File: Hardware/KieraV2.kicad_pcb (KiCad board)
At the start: 2 copper layers, 111 x 63.2 mm, 110 parts, among them J1 Conn_01x04_Male, J2 Conn_01x06_Male, SW1 SW_Rotary2x4, SW10 SW_Push, SW11 SW_Push, SW2 SW_Rotary2x4, SW3 SW_Push, SW4 SW_Push, SW5 SW_Push, SW6 SW_Push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

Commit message: refilled gnd again
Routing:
- net GND: vias 90 -> 171
- net (no net): vias 0 -> 11
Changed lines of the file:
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@@
     (thickness 1.6)
     (drawings 31)
-    (tracks 767)
+    (tracks 860)
     (zones 0)
     (modules 110)
@@
   (gr_line (start 105.5 89.8) (end 210.5 89.8) (layer Edge.Cuts) (width 0.1))
   (gr_line (start 102.5 92.8) (end 102.5 150) (layer Edge.Cuts) (width 0.1))
+  (via (at 191.99 94.025) (size 0.8) (drill 0.4) (layers F.Cu B.Cu) (net 0))
+  (via (at 195.01 95.565) (size 0.8) (drill 0.4) (layers F.Cu B.Cu) (net 0))
+  (via (at 197 92.575) (size 0.8) (drill 0.4) (layers F.Cu B.Cu) (net 0))
+  (via (at 188.02 92.875) (size 0.8) (drill 0.4) (layers F.Cu B.Cu) (net 0))
+  (via (at 191.11 99.015) (size 0.8) (drill 0.4) (layers F.Cu B.Cu) (net 0))
+  (via (at 186.3 99.505) (size 0.8) (drill 0.4) (layers F.Cu B.Cu) (net 0))
+  (via (at 183.16 99.015) (size 0.8) (drill 0.4) (layers F.Cu B.Cu) (net 0))
+  (via (at 175.51 105.285) (size 0.8) (drill 0.4) (layers F.Cu B.Cu) (net 0))
+  (via (at 180.14 105.205) (size 0.8) (drill 0.4) (layers F.Cu B.Cu) (net 0))
+  (via (at 209.89 92.025) (size 0.8) (drill 0.4) (layers F.Cu B.Cu) (net 0))
+  (via (at 175.59 112.12) (size 0.8) (drill 0.4) (layers F.Cu B.Cu) (net 0))
   (segment (start 154.6 109.840702) (end 154.6 109.8) (width 0.25) (layer F.Cu) (net 1))
   (segment (start 155.884298 111.125) (end 154.6 109.840702) (width 0.25) (layer F.Cu) (net 1))
@@
   (segment (start 151.3 109.8) (end 149.97 109.8) (width 0.25) (layer F.Cu) (net 1))
   (segment (start 149.97 109.8) (end 149.76 110.01) (width 0.25) (layer F.Cu) (net 1))
+  (via (at 149.19 111.42) (size 0.8) (drill 0.4) (layers F.Cu B.Cu) (net 1))
+  (via (at 152.25 112.7) (size 0.8) (drill 0.4) (layers F.Cu B.Cu) (net 1))
+  (via (at 150.04 112.25) (size 0.8) (drill 0.4) (layers F.Cu B.Cu) (net 1))
+  (via (at 146.75 107.96) (size 0.8) (drill 0.4) (layers F.Cu B.Cu) (net 1))
+  (via (at 153.77 107.32) (size 0.8) (drill 0.4) (layers F.Cu B.Cu) (net 1))
+  (via (at 159.25 110.81) (size 0.8) (drill 0.4) (layers F.Cu B.Cu) (net 1))
+  (via (at 161.5 110.93) (size 0.8) (drill 0.4) (layers F.Cu B.Cu) (net 1))
+  (via (at 163.06 108.61) (size 0.8) (drill 0.4) (layers F.Cu B.Cu) (net 1))
+  (via (at 163.36 105.59) (size 0.8) (drill 0.4) (layers F.Cu B.Cu) (net 1))
+  (via (at 166.05 105.71) (size 0.8) (drill 0.4) (layers F.Cu B.Cu) (net 1))
+  (via (at 166.4 109.16) (size 0.8) (drill 0.4) (layers F.Cu B.Cu) (net 1))
+  (via (at 170.35 113.1) (size 0.8) (drill 0.4) (layers F.Cu B.Cu) (net 1))
+  (via (at 173.99 112.24) (size 0.8) (drill 0.4) (layers F.Cu B.Cu) (net 1))
+  (via (at 180.39 114.37) (size 0.8) (drill 0.4) (layers F.Cu B.Cu) (net 1))
+  (via (at 178.5 115.94) (size 0.8) (drill 0.4) (layers F.Cu B.Cu) (net 1))
+  (via (at 180.47 119.08) (size 0.8) (drill 0.4) (layers F.Cu B.Cu) (net 1))
+  (via (at 178.55 121.98) (size 0.8) (drill 0.4) (layers F.Cu B.Cu) (net 1))
+  (via (at 178.28 118.11) (size 0.8) (drill 0.4) (layers F.Cu B.Cu) (net 1))
+  (via (at 181.4 124.85) (size 0.8) (drill 0.4) (layers F.Cu B.Cu) (net 1))
+  (via (at 179.48 128.08) (size 0.8) (drill 0.4) (layers F.Cu B.Cu) (net 1))
+  (via (at 183.48 133.02) (size 0.8) (drill 0.4) (layers F.Cu B.Cu) (net 1))
+  (via (at 182.27 140.23) (size 0.8) (drill 0.4) (layers F.Cu B.Cu) (net 1))
+  (via (at 190.15 135.41) (size 0.8) (drill 0.4) (layers F.Cu B.Cu) (net 1))
+  (via (at 186.54 148.22) (size 0.8) (drill 0.4) (layers F.Cu B.Cu) (net 1))
+  (via (at 175.85 148.11) (size 0.8) (drill 0.4) (layers F.Cu B.Cu) (net 1))
+  (via (at 176.24 142.67) (size 0.8) (drill 0.4) (layers F.Cu B.Cu) (net 1))
+  (via (at 169.76 149.71) (size 0.8) (drill 0.4) (layers F.Cu B.Cu) (net 1))
+  (via (at 155.43 145.36) (size 0.8) (drill 0.4) (layers F.Cu B.Cu) (net 1))
+  (via (at 158.77 139.17) (size 0.8) (drill 0.4) (layers F.Cu B.Cu) (net 1))
+  (via (at 160.73 145.25) (size 0.8) (drill 0.4) (layers F.Cu B.Cu) (net 1))
+  (via (at 132.46 149.4) (size 0.8) (drill 0.4) (layers F.Cu B.Cu) (net 1))
+  (via (at 112.33 141.63) (size 0.8) (drill 0.4) (layers F.Cu B.Cu) (net 1))
+  (via (at 125.62 137.12) (size 0.8) (drill 0.4) (layers F.Cu B.Cu) (net 1))
+  (via (at 126.77 132.24) (size 0.8) (drill 0.4) (layers F.Cu B.Cu) (net 1))
+  (via (at 126.69 128.51) (size 0.8) (drill 0.4) (layers F.Cu B.Cu) (net 1))
+  (via (at 136.73 119) (size 0.8) (drill 0.4) (layers F.Cu B.Cu) (net 1))
+  (via (at 138.86 117.35) (size 0.8) (drill 0.4) (layers F.Cu B.Cu) (net 1))
+  (via (at 133.39 112.55) (size 0.8) (drill 0.4) (layers F.Cu B.Cu) (net 1))
+  (via (at 132.83 108.85) (size 0.8) (drill 0.4) (layers F.Cu B.Cu) (net 1))
+  (via (at 135.32 110.39) (size 0.8) (drill 0.4) (layers F.Cu B.Cu) (net 1))
+  (via (at 139.98 109.63) (size 0.8) (drill 0.4) (layers F.Cu B.Cu) (net 1))
+  (via (at 143.88 108.01) (size 0.8) (drill 0.4) (layers F.Cu B.Cu) (net 1))
+  (via (at 138.91 98.13) (size 0.8) (drill 0.4) (layers F.Cu B.Cu) (net 1))
+  (via (at 144.92 98.19) (size 0.8) (drill 0.4) (layers F.Cu B.Cu) (net 1))
+  (via (at 152.35 91.68) (size 0.8) (drill 0.4) (layers F.Cu B.Cu) (net 1))
+  (via (at 148.73 91.01) (size 0.8) (drill 0.4) (layers F.Cu B.Cu) (net 1))
+  (via (at 173.55 93.2) (size 0.8) (drill 0.4) (layers F.Cu B.Cu) (net 1))
+  (via (at 176.47 99.06) (size 0.8) (drill 0.4) (layers F.Cu B.Cu) (net 1))
+  (via (at 179.58 98.84) (size 0.8) (drill 0.4) (layers F.Cu B.Cu) (net 1))
+  (via (at 183.9 92.67) (size 0.8) (drill 0.4) (layers F.Cu B.Cu) (net 1))
+  (via (at 188.81 106.6) (size 0.8) (drill 0.4) (layers F.Cu B.Cu) (net 1))
+  (via (at 194.53 110.25) (size 0.8) (drill 0.4) (layers F.Cu B.Cu) (net 1))
+  (via (at 196.63 113.08) (size 0.8) (drill 0.4) (layers F.Cu B.Cu) (net 1))
+  (via (at 194.05 114.49) (size 0.8) (drill 0.4) (layers F.Cu B.Cu) (net 1))
+  (via (at 196.6 122.9) (size 0.8) (drill 0.4) (layers F.Cu B.Cu) (net 1))
+  (via (at 199.35 125.25) (size 0.8) (drill 0.4) (layers F.Cu B.Cu) (net 1))
+  (via (at 210.15 126.15) (size 0.8) (drill 0.4) (layers F.Cu B.Cu) (net 1))
+  (via (at 210.46 134.85) (size 0.8) (drill 0.4) (layers F.Cu B.Cu) (net 1))
+  (via (at 203.33 131.85) (size 0.8) (drill 0.4) (layers F.Cu B.Cu) (net 1))
+  (via (at 199.49 141.66) (size 0.8) (drill 0.4) (layers F.Cu B.Cu) (net 1))
+  (via (at 197.11 147.66) (size 0.8) (drill 0.4) (layers F.Cu B.Cu) (net 1))
+  (via (at 191.86 121.55) (size 0.8) (drill 0.4) (layers F.Cu B.Cu) (net 1))
+  (via (at 211.03 105.16) (size 0.8) (drill 0.4) (layers F.Cu B.Cu) (net 1))
+  (via (at 210.39 96.51) (size 0.8) (drill 0.4) (layers F.Cu B.Cu) (net 1))
+  (via (at 188.8 97.29) (size 0.8) (drill 0.4) (layers F.Cu B.Cu) (net 1))
+  (via (at 193.27 95.32) (size 0.8) (drill 0.4) (layers F.Cu B.Cu) (net 1))
+  (via (at 197.42 96.02) (size 0.8) (drill 0.4) (layers F.Cu B.Cu) (net 1))
+  (via (at 186.96 94.39) (size 0.8) (drill 0.4) (layers F.Cu B.Cu) (net 1))
+  (via (at 194.77 102.24) (size 0.8) (drill 0.4) (layers F.Cu B.Cu) (net 1))
+  (via (at 124.21 105.41) (size 0.8) (drill 0.4) (layers F.Cu B.Cu) (net 1))
+  (via (at 125.85 100.57) (size 0.8) (drill 0.4) (layers F.Cu B.Cu) (net 1))
+  (via (at 129.22 101.27) (size 0.8) (drill 0.4) (layers F.Cu B.Cu) (net 1))
+  (via (at 124.07 96.5) (size 0.8) (drill 0.4) (layers F.Cu B.Cu) (net 1))
+  (via (at 121.36 92.48) (size 0.8) (drill 0.4) (layers F.Cu B.Cu) (net 1))
+  (via (at 128.91 92.53) (size 0.8) (drill 0.4) (layers F.Cu B.Cu) (net 1))
+  (via (at 124.67 112.26) (size 0.8) (drill 0.4) (layers F.Cu B.Cu) (net 1))
+  (via (at 119.31 116.74) (size 0.8) (drill 0.4) (layers F.Cu B.Cu) (net 1))
+  (via (at 119.68 124.22) (size 0.8) (drill 0.4) (layers F.Cu B.Cu) (net 1))
+  (via (at 110.38 115.06) (size 0.8) (drill 0.4) (layers F.Cu B.Cu) (net 1))
+  (via (at 113.51 127.66) (size 0.8) (drill 0.4) (layers F.Cu B.Cu) (net 1))
+  (via (at 115.12 124.5) (size 0.8) (drill 0.4) (layers F.Cu B.Cu) (net 1))
   (segment (start 152.525 104.775) (end 152.85 105.1) (width 0.25) (layer F.Cu) (net 2))
   (segment (start 151.05 104.775) (end 152.525 104.775) (width 0.25) (layer F.Cu) (net 2))
@@
   (segment (start 183.39 100.835) (end 191.725 92.5) (width 0.25) (layer F.Cu) (net 83))
   (segment (start 183.39 103.09) (end 183.39 100.835) (width 0.25) (layer F.Cu) (net 83))
-  (segment (start 193.55 95.875) (end 195.075 97.4) (width 0.25) (layer F.Cu) (net 84))
-  (segment (start 191.75 95.875) (end 193.55 95.875) (width 0.25) (layer F.Cu) (net 84))
   (segment (start 195.075 97.4) (end 196.75 97.4) (width 0.25) (layer F.Cu) (net 84))
   (via (at 172.25 110.191646) (size 0.8) (drill 0.4) (layers F.Cu B.Cu) (net 84))
@@
   (segment (start 171.7899 110.191646) (end 171.698263 110.100009) (width 0.25) (layer F.Cu) (net 84))
   (segment (start 172.25 110.191646) (end 171.7899 110.191646) (width 0.25) (layer F.Cu) (net 84))
+  (segment (start 192.075 96.2) (end 193.875 96.2) (width 0.25) (layer F.Cu) (net 84))
+  (segment (start 193.875 96.2) (end 195.075 97.4) (width 0.25) (layer F.Cu) (net 84))
+  (segment (start 191.75 95.875) (end 192.075 96.2) (width 0.25) (layer F.Cu) (net 84))
   (segment (start 195.175 99.85) (end 195.15 99.875) (width 0.25) (layer F.Cu) (net 85))
   (segment (start 196.75 99.85) (end 195.175 99.85) (width 0.25) (layer F.Cu) (net 85))

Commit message: refilled gnd again
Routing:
- net GND: track 27.1 -> 29.4 mm, vias 171 -> 172
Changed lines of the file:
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@@
     (thickness 1.6)
     (drawings 31)
-    (tracks 860)
+    (tracks 861)
     (zones 0)
     (modules 110)
@@
   (via (at 113.51 127.66) (size 0.8) (drill 0.4) (layers F.Cu B.Cu) (net 1))
   (via (at 115.12 124.5) (size 0.8) (drill 0.4) (layers F.Cu B.Cu) (net 1))
+  (segment (start 125.85 107.05) (end 124.21 105.41) (width 0.25) (layer F.Cu) (net 1))
+  (via (at 129.5 106.97) (size 0.8) (drill 0.4) (layers F.Cu B.Cu) (net 1))
   (segment (start 152.525 104.775) (end 152.85 105.1) (width 0.25) (layer F.Cu) (net 2))
   (segment (start 151.05 104.775) (end 152.525 104.775) (width 0.25) (layer F.Cu) (net 2))
@@
   (segment (start 122.85 107.05) (end 124.2 107.05) (width 0.25) (layer F.Cu) (net 79))
   (segment (start 121 105.2) (end 122.85 107.05) (width 0.25) (layer F.Cu) (net 79))
-  (segment (start 124.2 107.05) (end 124.6 107.05) (width 0.25) (layer F.Cu) (net 79))
   (segment (start 165.783506 111.625) (end 165.061287 110.902781) (width 0.25) (layer F.Cu) (net 79))
   (via (at 165.061287 110.902781) (size 0.8) (drill 0.4) (layers F.Cu B.Cu) (net 79))

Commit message: refilled gnd again
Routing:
- net GND: vias 172 -> 180
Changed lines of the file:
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@@
     (thickness 1.6)
     (drawings 31)
-    (tracks 861)
+    (tracks 869)
     (zones 0)
     (modules 110)
@@
   (segment (start 125.85 107.05) (end 124.21 105.41) (width 0.25) (layer F.Cu) (net 1))
   (via (at 129.5 106.97) (size 0.8) (drill 0.4) (layers F.Cu B.Cu) (net 1))
+  (via (at 191.99 97.47) (size 0.8) (drill 0.4) (layers F.Cu B.Cu) (net 1))
+  (via (at 192.42 98.72) (size 0.8) (drill 0.4) (layers F.Cu B.Cu) (net 1))
+  (via (at 195.86 98.65) (size 0.8) (drill 0.4) (layers F.Cu B.Cu) (net 1))
+  (via (at 199.96 98.65) (size 0.8) (drill 0.4) (layers F.Cu B.Cu) (net 1))
+  (via (at 200.23 96.04) (size 0.8) (drill 0.4) (layers F.Cu B.Cu) (net 1))
+  (via (at 200.23 101.35) (size 0.8) (drill 0.4) (layers F.Cu B.Cu) (net 1))
+  (via (at 197.35 101.1) (size 0.8) (drill 0.4) (layers F.Cu B.Cu) (net 1))
+  (via (at 189.28 99.93) (size 0.8) (drill 0.4) (layers F.Cu B.Cu) (net 1))
   (segment (start 152.525 104.775) (end 152.85 105.1) (width 0.25) (layer F.Cu) (net 2))
   (segment (start 151.05 104.775) (end 152.525 104.775) (width 0.25) (layer F.Cu) (net 2))

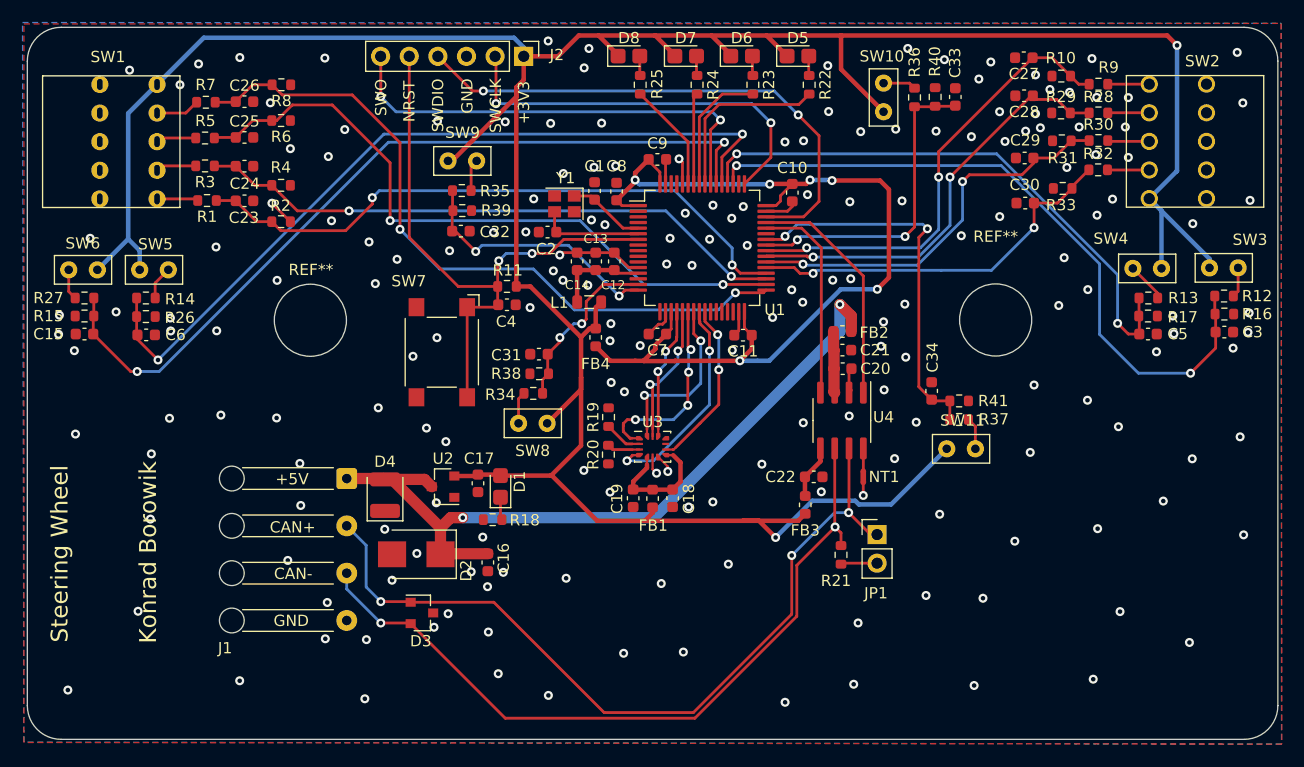
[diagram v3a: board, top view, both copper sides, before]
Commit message: changed positions for buttons
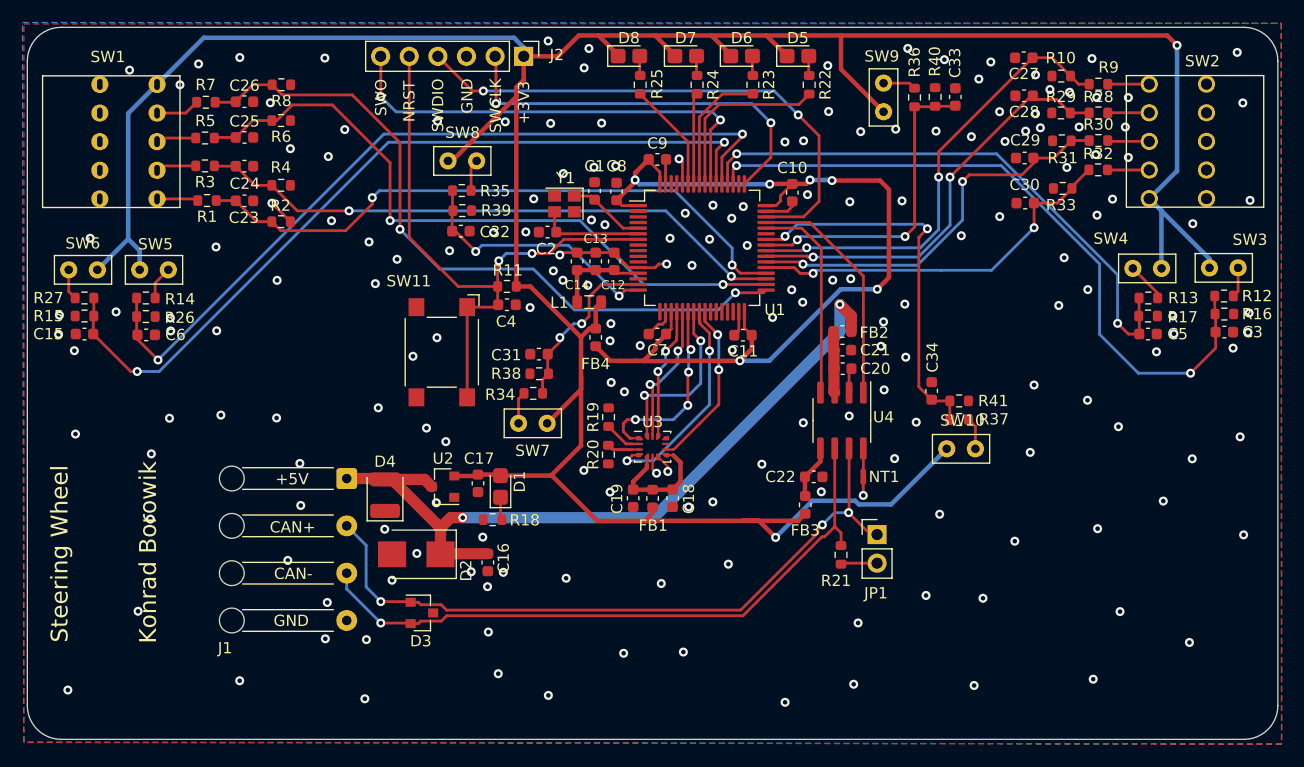
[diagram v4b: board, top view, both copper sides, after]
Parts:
- removed REF** (x2): MountingHole_6.4mm_M6, MountingHole:MountingHole_6.4mm_M6
- renumbered SW11 to SW10, SW7 to SW11, SW8 to SW7, SW9 to SW8, SW10 to SW9
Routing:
- net /CAN+: track 73.0 -> 62.6 mm
- net /CAN-: track 68.0 -> 58.4 mm, vias 2 -> 1
- net GND: track 29.4 -> 32.0 mm, vias 180 -> 178

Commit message: bigger holes
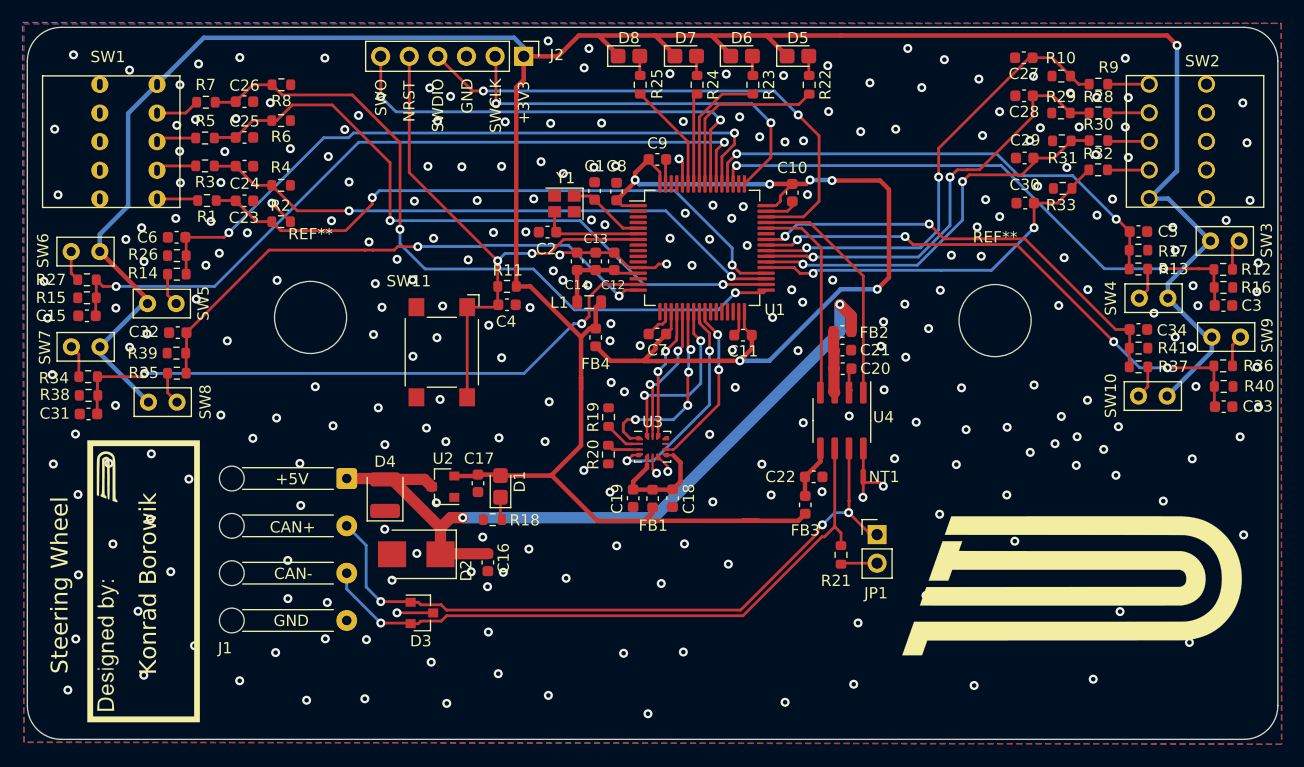
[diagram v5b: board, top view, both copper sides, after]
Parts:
- added G***: LOGO, Logos:SignatureBox25mm, F.Cu at (112.8, 139.0)
- added G***: LOGO, Logos:PUTM_LOGO_35mm, F.Cu at (194.3, 139.0)
- added REF**: MountingHole_6.4mm_M6, MountingHole:MountingHole_6.4mm_M6, F.Cu at (188.4, 115.8)
- added REF**: MountingHole_6.4mm_M6, MountingHole:MountingHole_6.4mm_M6, F.Cu at (127.6, 115.5)
- moved C31 40.3 mm to (107.9, 124.1)
- moved SW7 40.3 mm to (107.7, 118.2)
- moved R38 40.0 mm to (107.9, 122.5)
- moved R34 39.5 mm to (107.9, 120.8)
- moved SW9 37.1 mm to (208.9, 117.3), turned to 0 degrees
- moved C33 36.4 mm to (208.7, 123.5), turned to 0 degrees
- moved R36 36.3 mm to (208.6, 119.8), turned to 0 degrees
- moved R40 36.3 mm to (208.7, 121.7), turned to 180 degrees
- moved SW8 34.1 mm to (114.5, 123.1)
- moved R35 30.0 mm to (115.8, 120.5), turned to 180 degrees
- moved R39 28.3 mm to (115.7, 118.7), turned to 0 degrees
- moved C32 26.7 mm to (115.9, 116.9), turned to 180 degrees
- moved C34 19.1 mm to (201.1, 116.6), turned to 0 degrees
- moved SW10 17.7 mm to (202.4, 122.5), turned to 180 degrees
- moved R41 16.6 mm to (201.1, 118.3)
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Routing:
- net /SW7: track 15.6 -> 55.7 mm
- net /SW8: track 23.2 -> 48.9 mm
- net /SW9: track 28.2 -> 48.6 mm, vias 2 -> 4
- net +3V3: track 280.3 -> 265.2 mm, vias 2 -> 1
- net /SW5: track 71.6 -> 61.3 mm
- net /SW3: track 61.1 -> 51.2 mm
- net /SW4: track 51.1 -> 44.2 mm
- net /SW10: track 34.5 -> 40.2 mm
- net GND: track 32.0 -> 37.4 mm, vias 178 -> 278
- net /SW6: track 73.1 -> 68.6 mm
- net /NRST: track 53.7 -> 49.4 mm
- net /SW2_3: track 37.9 -> 39.0 mm
- net /SW1_1: track 63.0 -> 63.8 mm
- net Net-(R13-Pad2): track 3.53 -> 2.90 mm
- net (no net): vias 11 -> 0

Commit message: updated pcb
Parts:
- removed G***: LOGO, Logos:SignatureBox25mm
- removed G***: LOGO, Logos:PUTM_LOGO_35mm
- removed the REF** at (188.4, 115.8)
- removed the REF** at (127.6, 115.5)
- added D9: LED, Diode_SMD:D_0805_2012Metric_Castellated, F.Cu at (139.5, 130.2)
- added F1: Fuse_Small, Fuse:Fuse_1206_3216Metric, F.Cu at (134.0, 131.3)
- added R42: 1k, Resistor_SMD:R_0603_1608Metric, F.Cu at (138.5, 127.1)
- added REF**: MountingHole_6.4mm_M6, MountingHole:MountingHole_6.4mm_M6, F.Cu at (127.6, 115.8)
- added REF**: MountingHole_6.4mm_M6, MountingHole:MountingHole_6.4mm_M6, F.Cu at (188.4, 115.8)
- moved C16 10.6 mm to (140.5, 127.1), turned to 90 degrees
- moved D4 6.03 mm to (140.0, 133.1), turned to 180 degrees
- moved C17 4.81 mm to (147.3, 130.1)
- moved D1 4.81 mm to (149.3, 130.3)
- moved R18 4.81 mm to (148.6, 133.3)
- moved U2 4.81 mm to (144.2, 130.4)
- moved D2 0.63 mm to (136.7, 137.1)
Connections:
- C16 pad 1: +5V -> safe5V
- D2 pad 1: +5V -> safe5V
- D4 pad 2: +5V -> safe5V
- FB2 pad 1: +5V -> safe5V
- U2 pad 3: +5V -> safe5V
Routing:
- net +5V: track 69.0 -> 3.15 mm, vias 2 -> 0
- net safe5V: track 0.00 -> 63.4 mm, vias 0 -> 2
- net +3V3: track 265.2 -> 260.2 mm
- net Net-(D9-Pad1): track 0.00 -> 2.33 mm
- net GND: vias 278 -> 280
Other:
- board text added: "La, la, la, pudełko żółte, jakie piękne. La, la, la, pudełko jakieś żółte piękne. Moje żółte pudełko które znalazłem na plaży. Czemu jesteś takie żółciutkie jak piach? Prawie cię nie znalazłem, bo też byłoś żółte, jak piach wokół ciebie."
